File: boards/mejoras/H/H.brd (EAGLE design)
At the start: 100 x 45 mm, 3 parts, among them IC1 PIC18F4550_TQFP

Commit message: changes to g circuit
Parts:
- added JP3, JP4, JP5, JP6, JP7, JP8, JP9: (no value), pinhead:1X03
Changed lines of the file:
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@@
 <?xml version="1.0" encoding="utf-8"?>
 <!DOCTYPE eagle SYSTEM "eagle.dtd">
-<eagle version="9.6.2">
+<eagle version="9.6.0">
 <drawing>
 <settings>
@@
 <attribute name="VALUE" x="45.936" y="23.2299" size="1.778" layer="27"/>
 </element>
+<element name="JP3" library="pinhead" library_urn="urn:adsk.eagle:library:325" package="1X03" package3d_urn="urn:adsk.eagle:package:22458/2" value="" x="15" y="26" smashed="yes">
+<attribute name="NAME" x="11.1138" y="27.8288" size="1.27" layer="25" ratio="10"/>
+<attribute name="POPULARITY" value="92" x="15" y="26" size="1.778" layer="27" display="off"/>
+<attribute name="VALUE" x="11.19" y="22.825" size="1.27" layer="27"/>
+</element>
+<element name="JP4" library="pinhead" library_urn="urn:adsk.eagle:library:325" package="1X03" package3d_urn="urn:adsk.eagle:package:22458/2" value="" x="15" y="31" smashed="yes">
+<attribute name="NAME" x="11.1138" y="32.8288" size="1.27" layer="25" ratio="10"/>
+<attribute name="POPULARITY" value="92" x="15" y="31" size="1.778" layer="27" display="off"/>
+<attribute name="VALUE" x="11.19" y="27.825" size="1.27" layer="27"/>
+</element>
+<element name="JP5" library="pinhead" library_urn="urn:adsk.eagle:library:325" package="1X03" package3d_urn="urn:adsk.eagle:package:22458/2" value="" x="35" y="13" smashed="yes" rot="R270">
+<attribute name="NAME" x="36.8288" y="16.8862" size="1.27" layer="25" ratio="10" rot="R270"/>
+<attribute name="POPULARITY" value="92" x="35" y="13" size="1.778" layer="27" rot="R270" display="off"/>
+<attribute name="VALUE" x="31.825" y="16.81" size="1.27" layer="27" rot="R270"/>
+</element>
+<element name="JP6" library="pinhead" library_urn="urn:adsk.eagle:library:325" package="1X03" package3d_urn="urn:adsk.eagle:package:22458/2" value="" x="31" y="13" smashed="yes" rot="R90">
+<attribute name="NAME" x="29.1712" y="9.1138" size="1.27" layer="25" ratio="10" rot="R90"/>
+<attribute name="POPULARITY" value="92" x="31" y="13" size="1.778" layer="27" rot="R90" display="off"/>
+<attribute name="VALUE" x="34.175" y="9.19" size="1.27" layer="27" rot="R90"/>
+</element>
+<element name="JP7" library="pinhead" library_urn="urn:adsk.eagle:library:325" package="1X03" package3d_urn="urn:adsk.eagle:package:22458/2" value="" x="27" y="13" smashed="yes" rot="R90">
+<attribute name="NAME" x="25.1712" y="9.1138" size="1.27" layer="25" ratio="10" rot="R90"/>
+<attribute name="POPULARITY" value="92" x="27" y="13" size="1.778" layer="27" rot="R90" display="off"/>
+<attribute name="VALUE" x="30.175" y="9.19" size="1.27" layer="27" rot="R90"/>
+</element>
+<element name="JP8" library="pinhead" library_urn="urn:adsk.eagle:library:325" package="1X03" package3d_urn="urn:adsk.eagle:package:22458/2" value="" x="23" y="13" smashed="yes" rot="R270">
+<attribute name="NAME" x="24.8288" y="16.8862" size="1.27" layer="25" ratio="10" rot="R270"/>
+<attribute name="POPULARITY" value="92" x="23" y="13" size="1.778" layer="27" rot="R270" display="off"/>
+<attribute name="VALUE" x="19.825" y="16.81" size="1.27" layer="27" rot="R270"/>
+</element>
+<element name="JP9" library="pinhead" library_urn="urn:adsk.eagle:library:325" package="1X03" package3d_urn="urn:adsk.eagle:package:22458/2" value="" x="19" y="13" smashed="yes" rot="R270">
+<attribute name="NAME" x="20.8288" y="16.8862" size="1.27" layer="25" ratio="10" rot="R270"/>
+<attribute name="POPULARITY" value="92" x="19" y="13" size="1.778" layer="27" rot="R270" display="off"/>
+<attribute name="VALUE" x="15.825" y="16.81" size="1.27" layer="27" rot="R270"/>
+</element>
 </elements>

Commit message: udpated new circuits
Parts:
- added C1, C2: (no value), adafruit:C0805K
- added JP10: (no value), pinhead-enhanced:1X04/90
- added JP11: (no value), pinhead-enhanced-3:1X05/90
- added JP13: (no value), pinhead-enhanced-3:1X09/90
- added LED1: (no value), adafruit:CHIPLED_1206
- added Q1: (no value), crystal:HC49/S
- added R1, R2: 10k, adafruit:M1206
- added R3: 220, adafruit:M1206
- IC1: value PIC18F4550_TQFP -> PIC18F4455_TQFP
- JP3, JP4, JP5, JP6, JP7, JP9: device pinhead:1X03 -> pinhead-enhanced:1X04/90
- JP8: device pinhead:1X03 -> pinhead-enhanced-2:1X06/90
- moved JP9 78.8 mm to (97.5, 20.0)
- moved JP7 48.1 mm to (70.0, 34.5), turned to 0 degrees
- moved JP6 33.7 mm to (57.0, 34.5), turned to 0 degrees
- moved JP5 22.9 mm to (43.0, 34.5), turned to 0 degrees
- moved JP8 21.7 mm to (2.00, 18.5), turned to 90 degrees
- moved JP3 16.4 mm to (29.0, 34.5)
- moved IC1 9.06 mm to (51.0, 16.0), turned to 270 degrees
- moved JP4 3.54 mm to (15.5, 34.5)
- moved JP1 0.94 mm to (42.0, 0.00)
- moved JP2 0.80 mm to (65.0, 0.00)
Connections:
- removed net VDD: IC1.28, IC1.7
- removed net VSS: IC1.29, IC1.6
- new net 5V: IC1.28, IC1.7, JP1.3, JP10.3, JP11.1, JP3.3, JP4.3, JP5.3, JP6.3, JP7.3, JP8.3, JP9.3, R3.2
- new net B1: JP13.1
- new net B2: JP13.3
- new net CNY1: IC1.20, JP9.4
- new net CNY2: IC1.21, JP10.4
- new net GND: C1.2, C2.2, IC1.29, IC1.6, JP1.1, JP10.1, JP11.3, JP3.1, JP4.1, JP5.1, JP6.1, JP7.1, JP8.1, JP9.1, LED1.C, R1.1, R2.1
- new net IN1A: IC1.39, JP2.1
- new net IN1B: IC1.38, JP2.3
- new net IN2A: IC1.35, JP2.5
- new net IN2B: IC1.32, JP2.6
- new net LED1: JP13.5
- new net LED2: JP13.6
- new net LED3: JP13.7
- new net LED4: JP13.8
- new net LED5: JP13.9
- new net MCRL: IC1.18, JP8.4
- new net N$1: C1.1, IC1.31, Q1.2
- new net N$2: C2.1, IC1.30, Q1.1
- new net N$3: LED1.A, R3.1
- new net PGC: IC1.16, JP8.6
- new net PGD: IC1.17, JP8.5
- new net POT: JP13.4
- new net PWM1: IC1.36, JP2.4, R1.2
- new net PWM2: IC1.11, JP2.7, R2.2
- new net RX: IC1.1, JP11.4
- new net S1: IC1.5, JP3.4
- new net S2: JP4.4
- new net S3: JP5.4
- new net S4: JP6.4
- new net S5: JP7.4
- new net TX: IC1.44, JP11.5
- new net VPOWER_SENSE: IC1.19, JP2.8
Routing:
- net GND: track 0.00 -> 165.3 mm, vias 0 -> 2
- net 5V: track 0.00 -> 158.7 mm, vias 0 -> 1
- net PWM2: track 0.00 -> 39.1 mm, vias 0 -> 1
- net S1: track 0.00 -> 29.2 mm, vias 0 -> 1
- net VPOWER_SENSE: track 0.00 -> 26.5 mm, vias 0 -> 1
- net IN1A: track 0.00 -> 26.1 mm, vias 0 -> 1
- net IN1B: track 0.00 -> 21.6 mm, vias 0 -> 1
- net PWM1: track 0.00 -> 17.9 mm, vias 0 -> 1
- net IN2A: track 0.00 -> 13.6 mm, vias 0 -> 1
- net IN2B: track 0.00 -> 12.8 mm, vias 0 -> 1
- net N$3: track 0.00 -> 2.85 mm
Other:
- board size 100 x 45 mm -> 100 x 35 mm

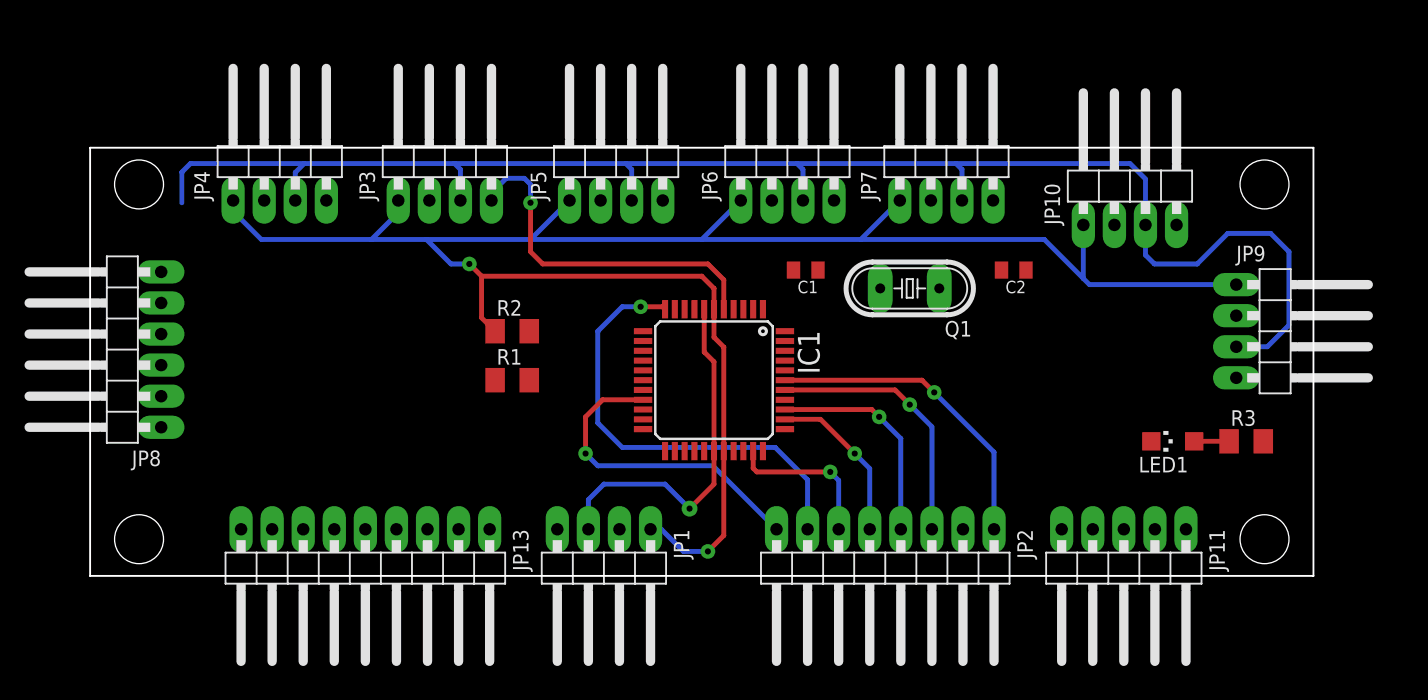
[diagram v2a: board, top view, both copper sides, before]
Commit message: added new sumo robot logic start board
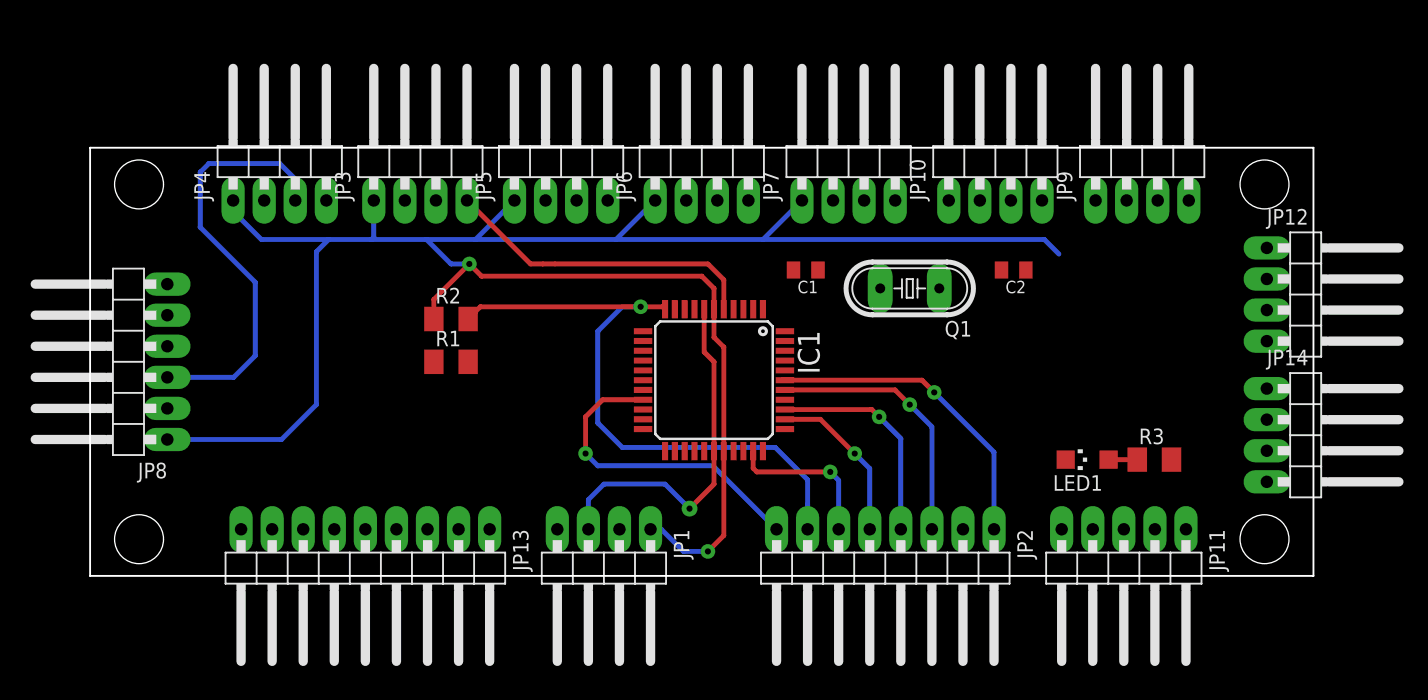
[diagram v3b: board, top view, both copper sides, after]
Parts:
- added JP12, JP14: (no value), pinhead-enhanced-3:1X04/90
- moved JP9 18.5 mm to (86.0, 34.5), turned to 0 degrees
- moved JP10 11.2 mm to (74.0, 34.5)
- moved JP7 8.00 mm to (62.0, 34.5)
- moved R3 7.65 mm to (87.0, 9.50)
- moved LED1 7.16 mm to (81.5, 9.50)
- moved JP6 7.00 mm to (50.0, 34.5)
- moved R1 5.22 mm to (29.5, 17.5)
- moved R2 5.10 mm to (29.5, 21.0)
- moved JP5 4.50 mm to (38.5, 34.5)
- moved JP3 2.00 mm to (27.0, 34.5)
- moved JP8 1.12 mm to (2.50, 17.5)
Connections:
- new net CNY3: IC1.22, JP12.4
- new net CNY4: IC1.24, JP14.4
- net 5V: now also JP12.3, JP14.3
- net B1: now also IC1.40
- net B2: now also IC1.41
- net GND: now also JP12.1, JP14.1
- net LED1: now also IC1.8
- net LED2: now also IC1.9
- net LED3: now also IC1.10
- net LED4: now also IC1.14
- net LED5: now also IC1.15
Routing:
- net 5V: track 158.7 -> 64.6 mm
- net PWM2: track 39.1 -> 53.6 mm
- net GND: track 165.3 -> 172.6 mm
- net S1: track 29.2 -> 26.1 mm, vias 1 -> 0
- net N$3: track 2.85 -> 2.35 mm

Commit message: added board h first version
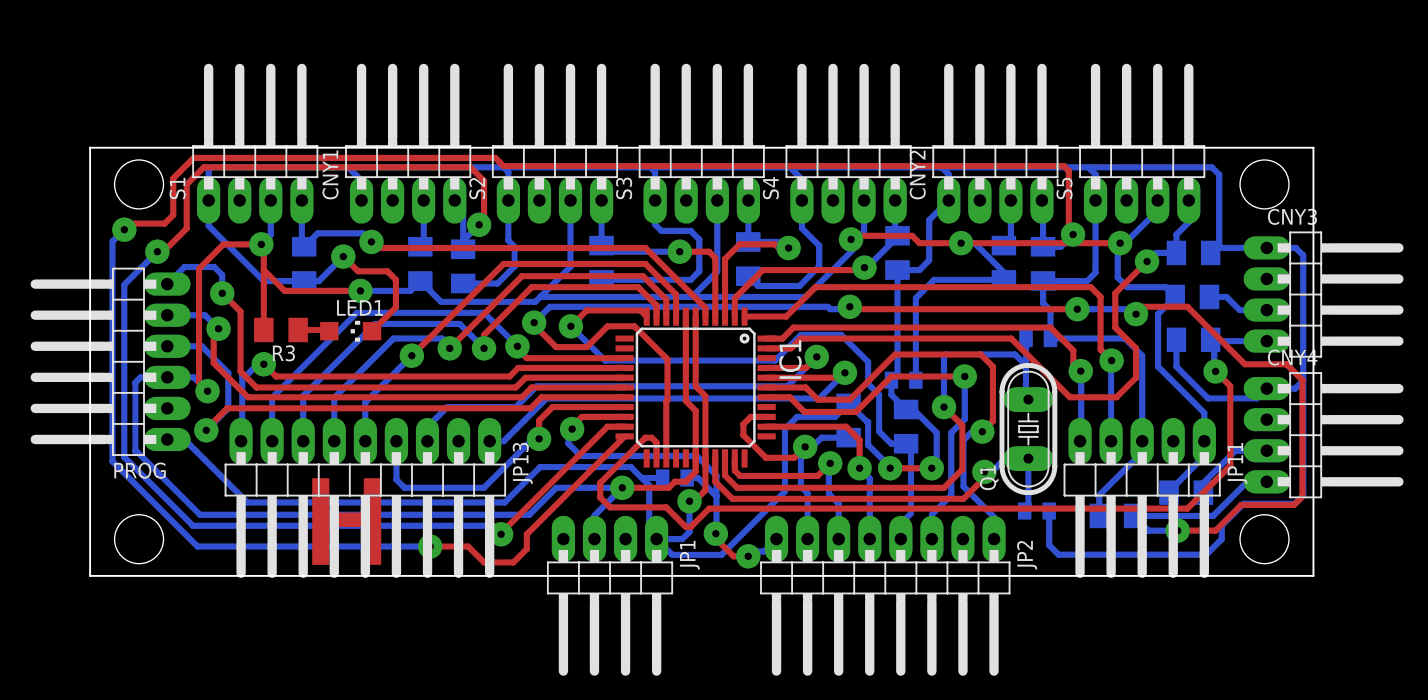
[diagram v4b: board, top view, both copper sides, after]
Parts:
- removed JP3, JP4, JP5: (no value), pinhead-enhanced:1X04/90
- added C3, C4: (no value), adafruit:C0805K
- added CNY1, S1, S2: (no value), pinhead-enhanced:1X04/90
- added R10, R11, R12, R4, R5, R6, R7, R8, R9: 10k, adafruit:M1206
- added R13, R14, R15, R16: 220, adafruit:M1206
- moved R3 72.2 mm to (15.6, 20.1), turned to 180 degrees
- moved LED1 61.1 mm to (21.3, 20.0), turned to 270 degrees
- moved R1 37.6 mm to (66.7, 12.2), flipped to the bottom, turned to 270 degrees
- moved R2 33.5 mm to (62.0, 12.7), flipped to the bottom, turned to 270 degrees
- moved C1 19.8 mm to (77.5, 19.4), flipped to the bottom
- moved C2 19.8 mm to (77.4, 5.30), flipped to the bottom
- moved Q1 15.0 mm to (76.7, 12.0), turned to 90 degrees
- moved JP11 7.35 mm to (86.0, 7.20)
- moved JP13 7.20 mm to (22.5, 7.20)
- moved IC1 1.62 mm to (49.5, 15.4)
- moved JP1 0.94 mm to (42.5, -0.80)
- moved JP2 0.80 mm to (65.0, -0.80)
- renumbered JP10 to CNY2, JP12 to CNY3, JP14 to CNY4, JP6 to S3, JP7 to S4, JP8 to PROG, JP9 to S5
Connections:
- new net N$4: CNY1.3, R13.2
- new net N$5: CNY2.3, R14.2
- new net N$6: CNY3.3, R15.2
- new net N$7: CNY4.3, R16.2
- net 5V: now also C3.1, R13.1, R14.1, R15.1, R16.1, S1.3, S2.3; no longer CNY2.3, CNY3.3, CNY4.3, JP3.3, JP4.3, JP5.3
- net CNY1: now also CNY1.4, IC1.21, R4.2; no longer IC1.20, S5.4
- net CNY2: now also IC1.22, R5.2; no longer IC1.21
- net CNY3: now also IC1.24, R6.2; no longer IC1.22
- net CNY4: now also IC1.25, R7.2; no longer IC1.24
- net GND: now also C3.2, C4.2, CNY1.1, R10.1, R11.1, R12.1, R4.1, R5.1, R6.1, R7.1, R8.1, R9.1, S1.1, S2.1; no longer JP3.1, JP4.1, JP5.1
- net POT: now also IC1.19
- net PWM1: now also IC1.11; no longer IC1.36
- net PWM2: now also IC1.36; no longer IC1.11
- net S1: now also R8.2, S1.4; no longer JP3.4
- net S2: now also IC1.4, R9.2, S2.4; no longer JP4.4
- net S3: now also IC1.3, R10.2, S3.4; no longer JP5.4
- net S4: now also IC1.2, R11.2, S4.4; no longer S3.4
- net S5: now also IC1.43, R12.2, S5.4; no longer S4.4
- net VPOWER_SENSE: now also C4.1, IC1.20; no longer IC1.19
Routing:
- net GND: track 172.6 -> 417.3 mm, vias 2 -> 4
- net 5V: track 64.6 -> 256.8 mm, vias 1 -> 7
- net CNY2: track 0.00 -> 163.5 mm, vias 0 -> 3
- net CNY4: track 0.00 -> 126.3 mm, vias 0 -> 5
- net CNY1: track 0.00 -> 107.8 mm, vias 0 -> 3
- net CNY3: track 0.00 -> 79.0 mm, vias 0 -> 1
- net S5: track 0.00 -> 51.9 mm, vias 0 -> 1
- net MCRL: track 0.00 -> 46.7 mm, vias 0 -> 1
- net PGC: track 0.00 -> 46.1 mm, vias 0 -> 1
- net N$1: track 0.00 -> 43.9 mm, vias 0 -> 1
- net PGD: track 0.00 -> 42.7 mm, vias 0 -> 1
- net RX: track 0.00 -> 42.6 mm, vias 0 -> 1
- net LED3: track 0.00 -> 40.1 mm, vias 0 -> 1
- net B2: track 0.00 -> 39.8 mm, vias 0 -> 1
- net B1: track 0.00 -> 37.9 mm, vias 0 -> 1
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
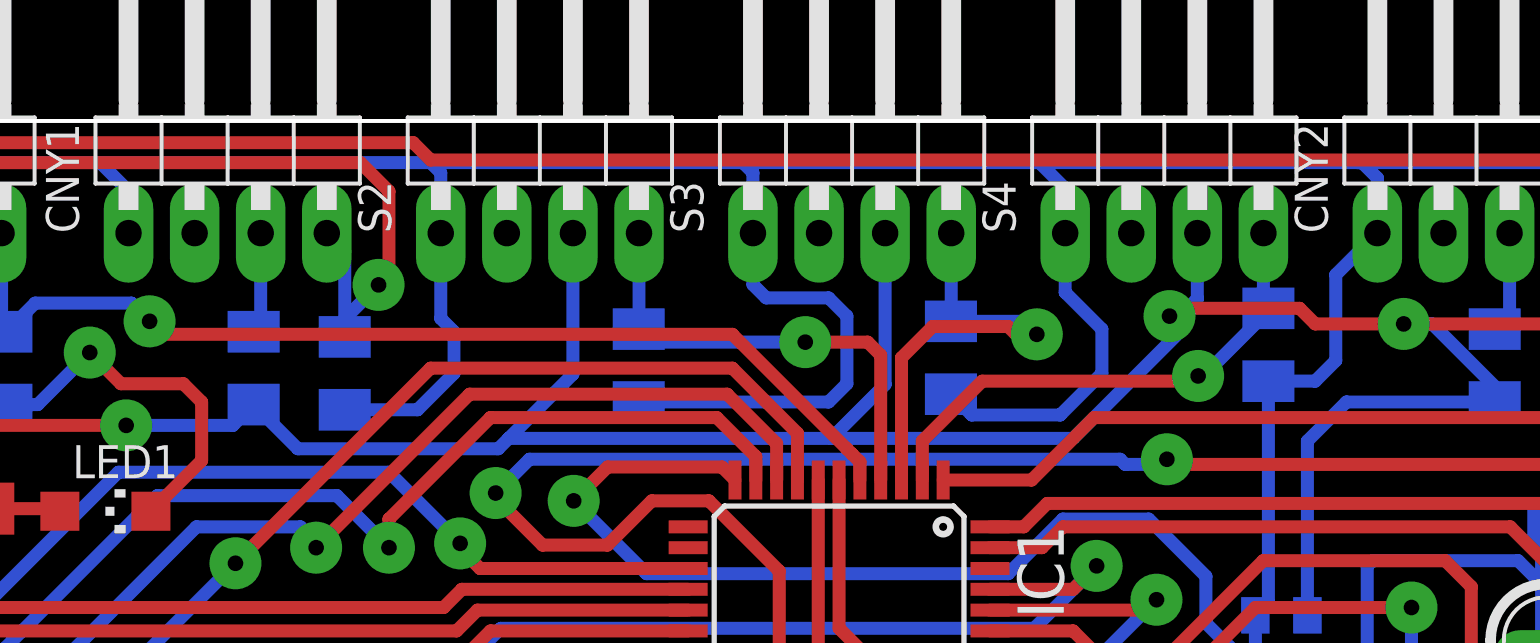
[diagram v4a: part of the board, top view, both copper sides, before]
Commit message: added circuit H and I
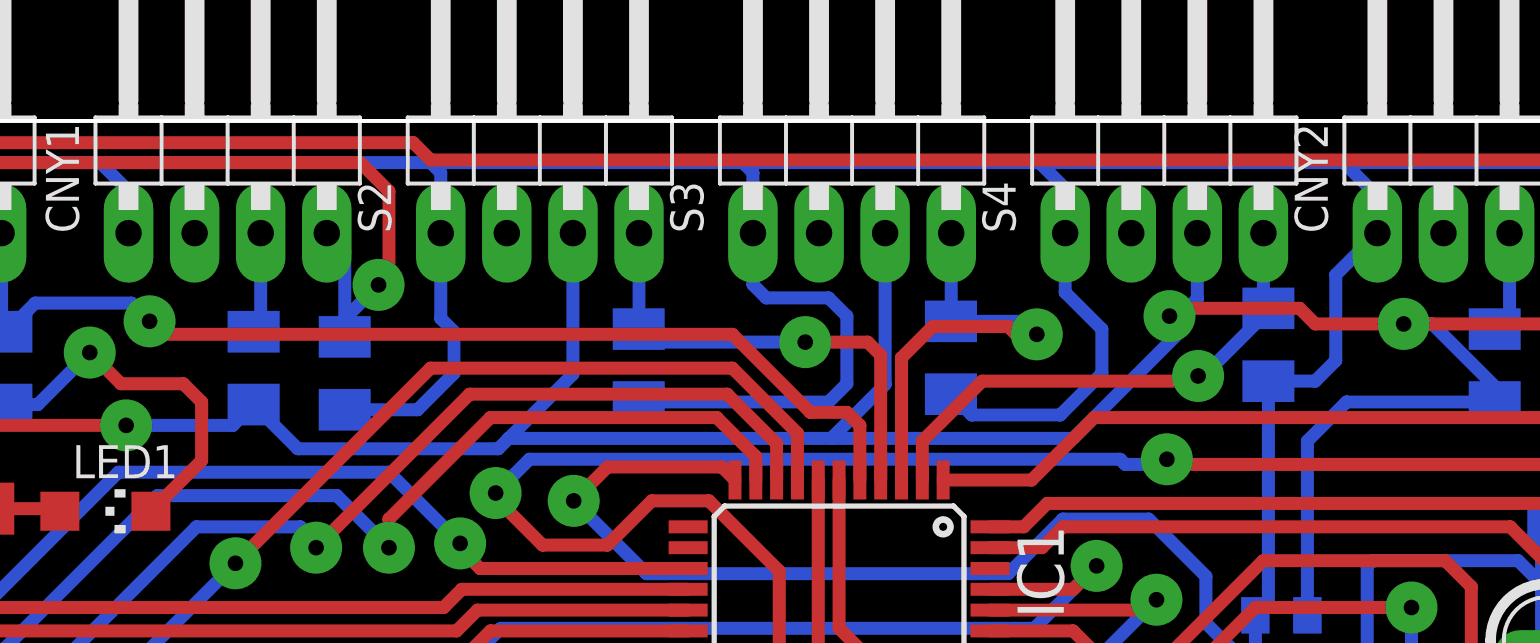
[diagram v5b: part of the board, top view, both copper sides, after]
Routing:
- net S1: track 40.4 -> 41.2 mm
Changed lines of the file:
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@@
 <wire x1="58.19" y1="32.41" x2="58.19" y2="30.69" width="0.5" layer="16"/>
 <wire x1="57.2" y1="33.4" x2="58.19" y2="32.41" width="0.5" layer="16"/>
-<wire x1="57.2" y1="33.4" x2="69.6" y2="33.4" width="0.5" layer="16"/>
-<wire x1="70.19" y1="32.81" x2="70.19" y2="30.69" width="0.5" layer="16"/>
-<wire x1="70.19" y1="32.81" x2="69.6" y2="33.4" width="0.5" layer="16"/>
+<wire x1="57.2" y1="33.4" x2="68.9" y2="33.4" width="0.5" layer="16"/>
+<wire x1="68.9" y1="33.4" x2="69.6" y2="33.4" width="0.5" layer="16"/>
 <wire x1="69.4" y1="33.4" x2="81.6" y2="33.4" width="0.5" layer="16"/>
 <wire x1="82.19" y1="32.81" x2="82.19" y2="30.69" width="0.5" layer="16"/>
@@
 <wire x1="45.71" y1="7.39" x2="45.1" y2="8" width="0.5" layer="16"/>
 <wire x1="45.71" y1="3.61" x2="45.71" y2="7.39" width="0.5" layer="16"/>
-<wire x1="70.19" y1="30.69" x2="69.4" y2="33.4" width="0" layer="19" extent="16-16"/>
+<wire x1="70.19" y1="30.69" x2="70.19" y2="32.11" width="0.5" layer="16"/>
+<wire x1="70.19" y1="32.11" x2="68.9" y2="33.4" width="0.5" layer="16"/>
+<wire x1="69.6" y1="33.4" x2="69.4" y2="33.4" width="0" layer="19" extent="16-16"/>
 </signal>
 <signal name="5V">
@@
 <wire x1="23" y1="27.3" x2="22.3" y2="28" width="0.5" layer="16"/>
 <via x="23" y="27.3" extent="1-16" drill="0.6" diameter="2"/>
-<wire x1="45.4" y1="26.8" x2="23.5" y2="26.8" width="0.5" layer="1"/>
+<wire x1="23.5" y1="26.8" x2="45.4" y2="26.8" width="0.5" layer="1"/>
 <wire x1="23" y1="27.3" x2="23.5" y2="26.8" width="0.5" layer="1"/>
-<wire x1="50.3" y1="21.9" x2="50.3" y2="21.2" width="0.5" layer="1"/>
-<wire x1="45.4" y1="26.8" x2="49.8" y2="22.4" width="0.5" layer="1"/>
-<wire x1="49.8" y1="22.4" x2="50" y2="22.2" width="0.5" layer="1"/>
-<wire x1="50" y1="22.2" x2="50.3" y2="21.9" width="0.5" layer="1"/>
+<wire x1="45.4" y1="26.8" x2="48.4" y2="23.8" width="0.5" layer="1"/>
+<wire x1="50.3" y1="23.3" x2="50.3" y2="21.2" width="0.5" layer="1"/>
+<wire x1="48.4" y1="23.8" x2="49.8" y2="23.8" width="0.5" layer="1"/>
+<wire x1="49.8" y1="23.8" x2="50.3" y2="23.3" width="0.5" layer="1"/>
 </signal>
 <signal name="S2">

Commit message: updated board h and i
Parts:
- moved R3 0.61 mm to (16.1, 20.5)
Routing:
- net CNY1: track 107.8 -> 102.1 mm
- net S1: track 41.2 -> 45.9 mm
- net 5V: track 256.8 -> 254.4 mm
- net PGC: track 46.1 -> 44.8 mm
- net CNY2: track 163.5 -> 162.3 mm
- net GND: track 417.6 -> 416.7 mm
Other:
- board text added: "C:/Users/Ariel/GitHub/Sumo-Robot-Programs-Database/boards/mejoras/I/1.bmp"
